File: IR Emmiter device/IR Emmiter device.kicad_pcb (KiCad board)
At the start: 2 copper layers, 251.5 x 76.2 mm, 56 parts, among them J1 USB_C_Receptacle_USB2.0, J2 ICSP Header, J3 AudioJack3_Ground_Switch, J4 AudioJack3_Ground_Switch, J5 AudioJack3_Ground_Switch, J6 External Power, J7 TOP LED CONNECTION, J8 Conn_01x02_Female, Q1 FDS6890A, Q2 FDS6890A, Q3 FDS6890A, Q4 FDS6890A, SW1 SW_Push, SW2 SW_Push, U1 LM7805_TO220, U2 ATmega328-PU, U3 CH330N, Y1 8 MHz

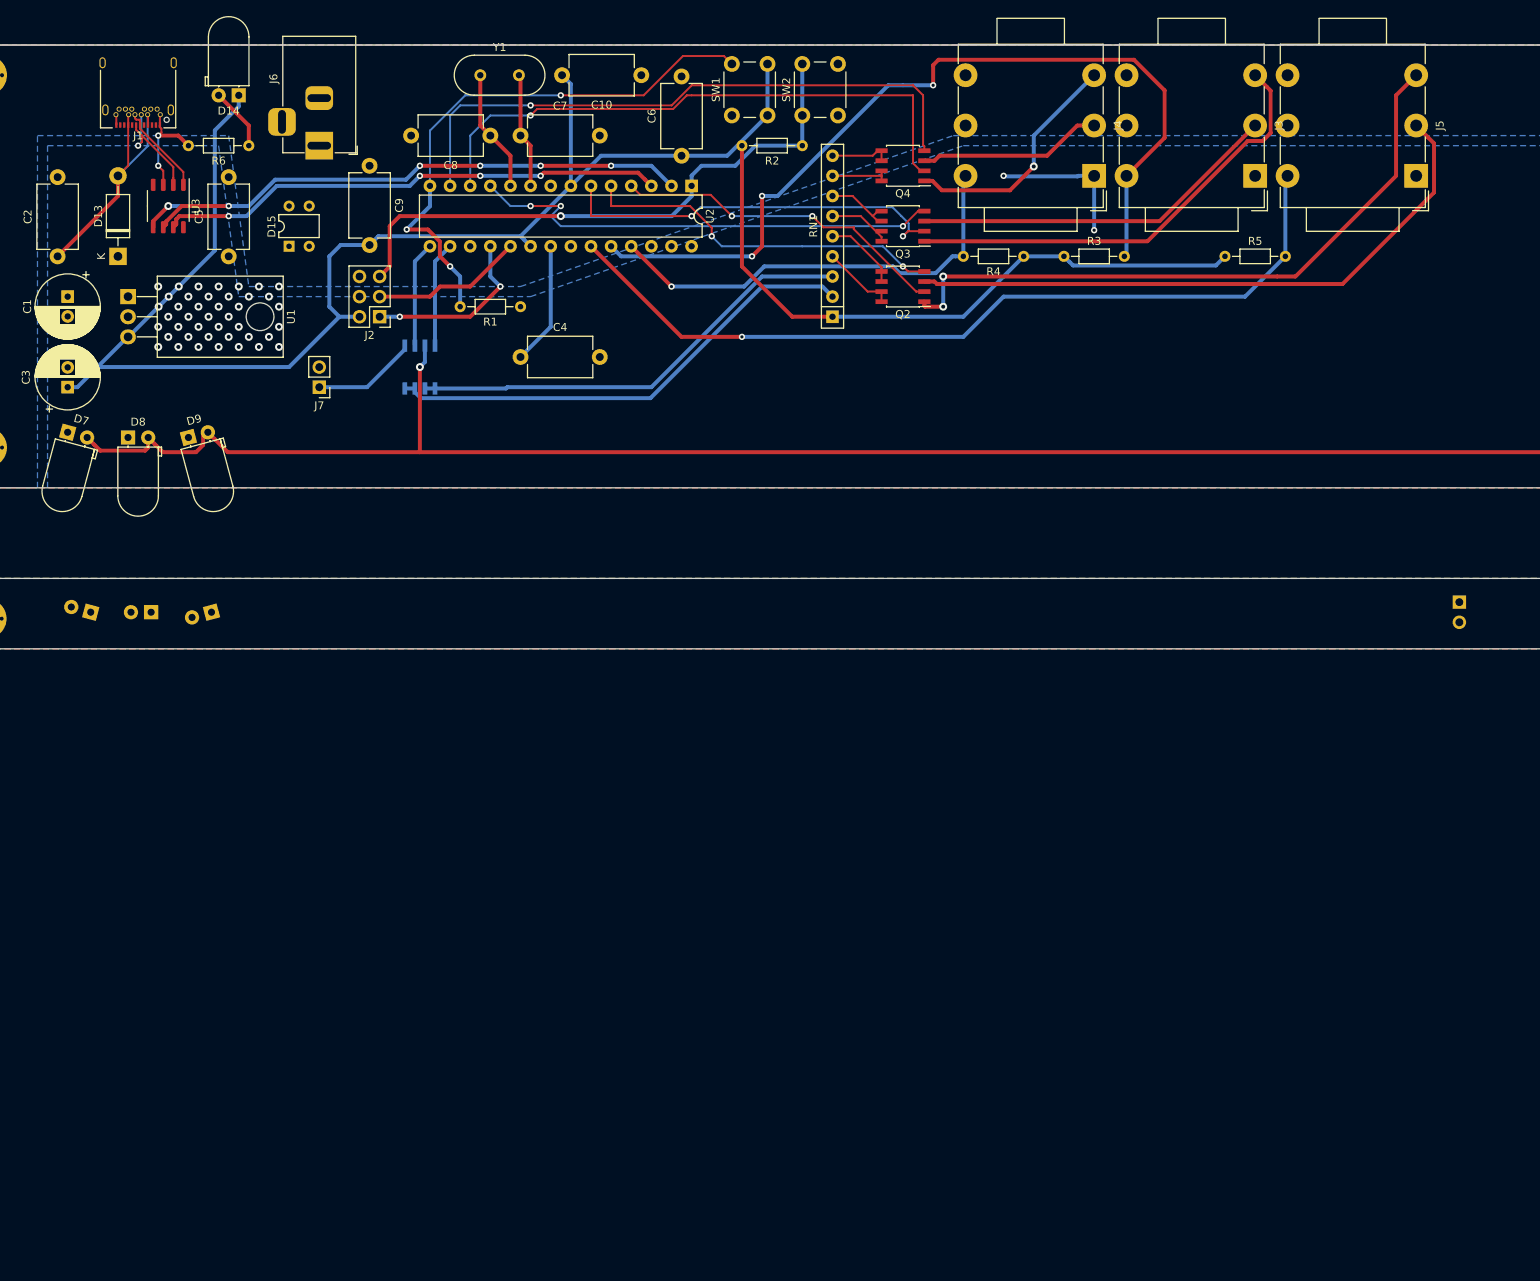
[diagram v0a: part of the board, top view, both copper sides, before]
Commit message: Minor changes to schematic, swapped out parts on PCB layout to aid in case design and added footprints for the expansions
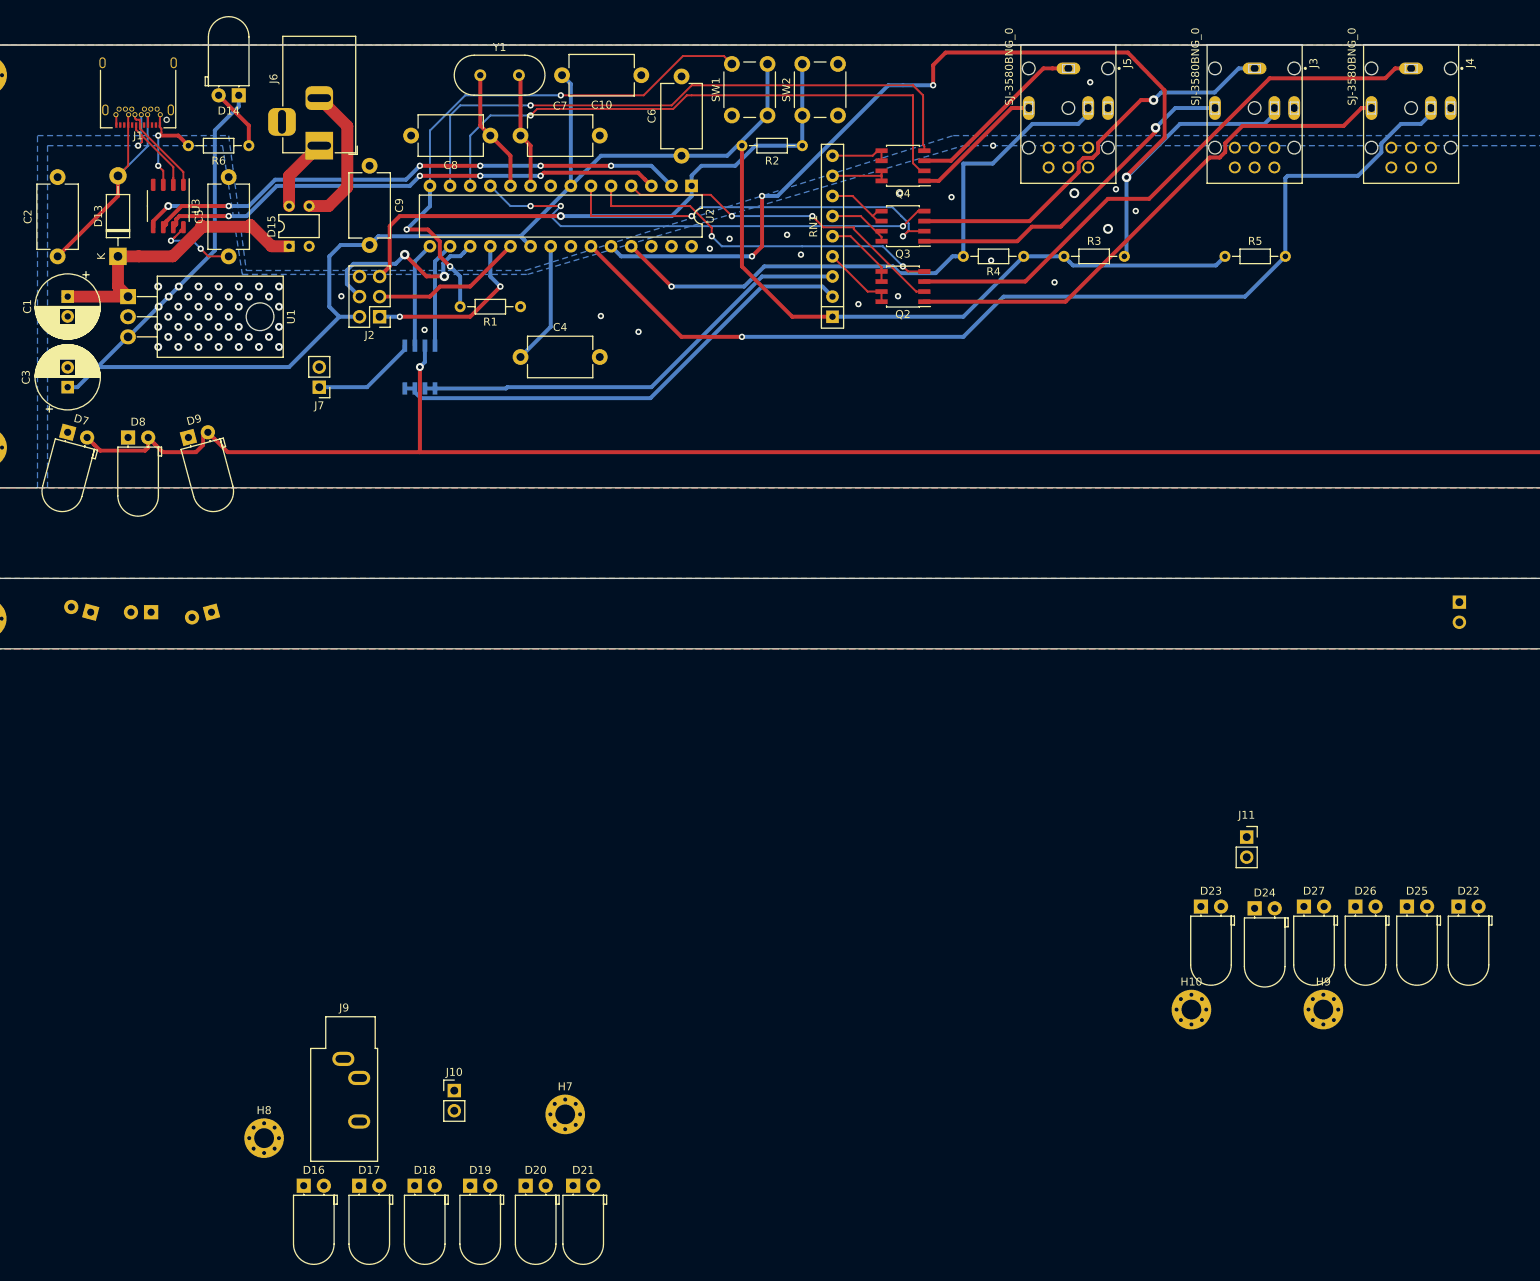
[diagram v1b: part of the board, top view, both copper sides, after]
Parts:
- added D16: LED_Small, LED_THT:LED_D5.0mm_Horizontal_O1.27mm_Z3.0mm_Clear, F.Cu at (59.0, 163.0)
- added D17: LED_Small, LED_THT:LED_D5.0mm_Horizontal_O1.27mm_Z3.0mm_Clear, F.Cu at (66.0, 163.0)
- added D18: LED_Small, LED_THT:LED_D5.0mm_Horizontal_O1.27mm_Z3.0mm_Clear, F.Cu at (73.0, 163.0)
- added D19: LED_Small, LED_THT:LED_D5.0mm_Horizontal_O1.27mm_Z3.0mm_Clear, F.Cu at (80.0, 163.0)
- added D20: LED_Small, LED_THT:LED_D5.0mm_Horizontal_O1.27mm_Z3.0mm_Clear, F.Cu at (87.0, 163.0)
- added D21: LED_Small, LED_THT:LED_D5.0mm_Horizontal_O1.27mm_Z3.0mm_Clear, F.Cu at (93.0, 163.0)
- added D22: LED_Small, LED_THT:LED_D5.0mm_Horizontal_O1.27mm_Z3.0mm_Clear, F.Cu at (204.7, 127.8)
- added D23: LED_Small, LED_THT:LED_D5.0mm_Horizontal_O1.27mm_Z3.0mm_Clear, F.Cu at (172.2, 127.8)
- added D24: LED_Small, LED_THT:LED_D5.0mm_Horizontal_O1.27mm_Z3.0mm_Clear, F.Cu at (179.0, 128.0)
- added D25: LED_Small, LED_THT:LED_D5.0mm_Horizontal_O1.27mm_Z3.0mm_Clear, F.Cu at (198.2, 127.8)
- added D26: LED_Small, LED_THT:LED_D5.0mm_Horizontal_O1.27mm_Z3.0mm_Clear, F.Cu at (191.7, 127.8)
- added D27: LED_Small, LED_THT:LED_D5.0mm_Horizontal_O1.27mm_Z3.0mm_Clear, F.Cu at (185.2, 127.8)
- added H10: MountingHole_Pad, MountingHole:MountingHole_2.5mm_Pad_Via, F.Cu at (171.0, 140.8)
- added H7: MountingHole_Pad, MountingHole:MountingHole_2.5mm_Pad_Via, F.Cu at (92.0, 154.0)
- added H8: MountingHole_Pad, MountingHole:MountingHole_2.5mm_Pad_Via, F.Cu at (54.0, 157.0)
- added H9: MountingHole_Pad, MountingHole:MountingHole_2.5mm_Pad_Via, F.Cu at (187.7, 140.8)
- added J10: TOP LED CONNECTION, Connector_PinHeader_2.54mm:PinHeader_1x02_P2.54mm_Vertical, F.Cu at (78.0, 151.0)
- added J11: Conn_01x02_Female, Connector_PinSocket_2.54mm:PinSocket_1x02_P2.54mm_Vertical, F.Cu at (178.0, 119.0)
- added J9: AudioJack3, Connector_Audio:Jack_3.5mm_CUI_SJ1-3533NG_Horizontal, F.Cu at (64.0, 147.0)
- J3, J4, J5: value AudioJack3_Ground_Switch -> SJ-3580BNG_0; footprint Connector_Audio:Jack_3.5mm_Neutrik_NMJ6HCD2_Horizontal -> Connector_Audio:SJ-3580BNG
- moved J5 44.1 mm to (155.5, 27.0)
- moved J4 40.2 mm to (198.8, 27.0)
- moved J3 4.14 mm to (179.0, 27.0)
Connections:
- Q2 pad 1: Net-(J5-PadT) -> Net-(J4-Pad2)
- Q2 pad 3: Net-(J5-PadR) -> Net-(J4-Pad1)
- Q3 pad 1: Net-(J3-PadT) -> Net-(J3-Pad2)
- Q3 pad 3: Net-(J3-PadR) -> Net-(J3-Pad1)
- Q4 pad 1: Net-(J4-PadT) -> Net-(J5-Pad2)
- Q4 pad 3: Net-(J4-PadR) -> Net-(J5-Pad1)
- R3 pad 2: Net-(J3-PadSN) -> Net-(J3-Pad11)
- R4 pad 2: Net-(J4-PadSN) -> Net-(J5-Pad11)
- R5 pad 2: Net-(J5-PadSN) -> Net-(J4-Pad11)
- U2 pad 23: Net-(J5-PadSN) -> Net-(J4-Pad11)
- U2 pad 24: Net-(J3-PadSN) -> Net-(J3-Pad11)
- U2 pad 25: Net-(J4-PadSN) -> Net-(J5-Pad11)
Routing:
- net Net-(J3-Pad11): track 0.00 -> 134.0 mm, vias 0 -> 4
- net Net-(J4-Pad11): track 0.00 -> 129.6 mm, vias 0 -> 1
- net Net-(J3-PadSN): track 110.5 -> 0.00 mm, vias 3 -> 0
- net Net-(J5-PadSN): track 106.8 -> 0.00 mm, vias 1 -> 0
- net Net-(J5-PadT): track 82.9 -> 0.00 mm, vias 2 -> 0
- net Net-(J5-PadR): track 78.6 -> 0.00 mm
- net Net-(J5-Pad11): track 0.00 -> 77.1 mm, vias 0 -> 1
- net Net-(J4-Pad1): track 0.00 -> 72.6 mm
- net Net-(J4-Pad2): track 0.00 -> 67.2 mm
- net Net-(J3-PadT): track 57.5 -> 0.00 mm
- net Net-(J4-PadSN): track 56.6 -> 0.00 mm, vias 1 -> 0
- net Net-(J3-Pad1): track 0.00 -> 51.0 mm, vias 0 -> 1
- net Net-(J3-PadR): track 46.7 -> 0.00 mm
- net Net-(J3-Pad2): track 0.00 -> 43.9 mm, vias 0 -> 1
- net Net-(C1-Pad1): track 0.00 -> 37.9 mm
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
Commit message: Completed basic shape of case for main unit, finished layout of PCB for improved sensor bar
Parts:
- added LOGO1: Logo_Open_Hardware_Large, Symbol:OSHW-Logo_5.7x6mm_SilkScreen, F.Cu at (261.0, 60.0)
- D22, D23, D24, D25, D26, D27, J11: moved to B.Cu
- J1: footprint Connector_USB:USB_C_Receptacle_Amphenol_12401548E4-2A -> Connector_USB:USB4085-GF-A_REVA
- moved H8 213.0 mm to (262.8, 114.5)
- moved D21 163.9 mm to (249.8, 115.2), turned to 15 degrees
- moved D19 163.4 mm to (236.0, 114.6), turned to 345 degrees
- moved D20 163.1 mm to (243.0, 115.2)
- moved D27 152.6 mm to (32.8, 134.5), turned to 165 degrees
- moved H10 152.3 mm to (19.0, 132.0)
- moved J8 143.9 mm to (61.0, 92.0), turned to 0 degrees
- moved D24 139.5 mm to (39.7, 134.6), turned to 180 degrees
- moved D23 125.9 mm to (46.4, 133.8), turned to 195 degrees
- moved J9 97.6 mm to (152.8, 106.5)
- moved H7 83.2 mm to (19.0, 114.0)
- moved J11 76.0 mm to (103.0, 131.2), turned to 180 degrees
- moved H9 75.6 mm to (262.8, 132.2)
- moved D26 60.8 mm to (252.2, 133.6), turned to 195 degrees
- moved D16 55.7 mm to (30.5, 115.1), turned to 345 degrees
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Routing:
- net Net-(J10-Pad1): track 0.00 -> 56.1 mm
- net GND: track 15.1 -> 40.2 mm, vias 61 -> 147
- net Earth: track 0.00 -> 15.9 mm
- net Net-(J7-Pad1): track 13.2 -> 19.7 mm
- net Net-(D15-Pad4): track 9.20 -> 3.81 mm
- net Net-(D15-Pad3): track 18.5 -> 13.5 mm
- net Net-(J1-PadA6): track 11.6 -> 15.2 mm
- net BOTTOM_LEDS: track 245.4 -> 247.6 mm
- net VBUS: track 32.2 -> 32.5 mm, vias 0 -> 2
- net Net-(J1-PadA7): track 15.0 -> 15.3 mm, vias 1 -> 0
- net +5V: vias 4 -> 1
- added copper zone on F.Cu, net Net-(D16-Pad1)
- added copper zone on B.Cu, net Net-(D16-Pad2)
- added copper zone on F.Cu, net Net-(D22-Pad1)
- added copper zone on B.Cu, net Net-(D22-Pad2)
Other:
- board size 251.5 x 76.2 mm -> 251.7 x 117.5 mm
- board text added: "ASSEMBLY INSTRUCTIONS"
- board text added: "Attach top and bottom boards with standoffs"
- board text added: "EARTH"
- board text added: "Expansion bottom"
- board text added: "Expansion top"
- board text added: "ICSP"
- board text added: "If using the case, insert the boards into it then attach the top cover"
- board text added: "MAIN BOARD CONNECTS HERE"
- board text added: "Main unit bottom"
- board text added: "Main unit top"
- board text added: "PWR / MODE"
- board text added: "RST"
- board text added: "SIGNAL GND"
- board text added: "Solder all components onto the board"
- board text added: "TOP LED ASSEMBLY CONNECTS HERE"
- board text added: "github.com/willlovesbearz/Advanced-wiimote-tracking/"
